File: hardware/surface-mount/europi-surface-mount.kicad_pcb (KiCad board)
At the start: 2 copper layers, 40.6 x 110 mm, 88 parts, among them J1 Conn_02x05_Odd_Even, J10 Output 6 Jack, J11 Conn_01x04_Pin, J2 Conn_01x04_Pin, J3 Output 1 Jack, J4 Output 4 Jack, J5 Analogue Input Jack, J6 Output 2 Jack, J7 Output 5 Jack, J8 Digital Input Jack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

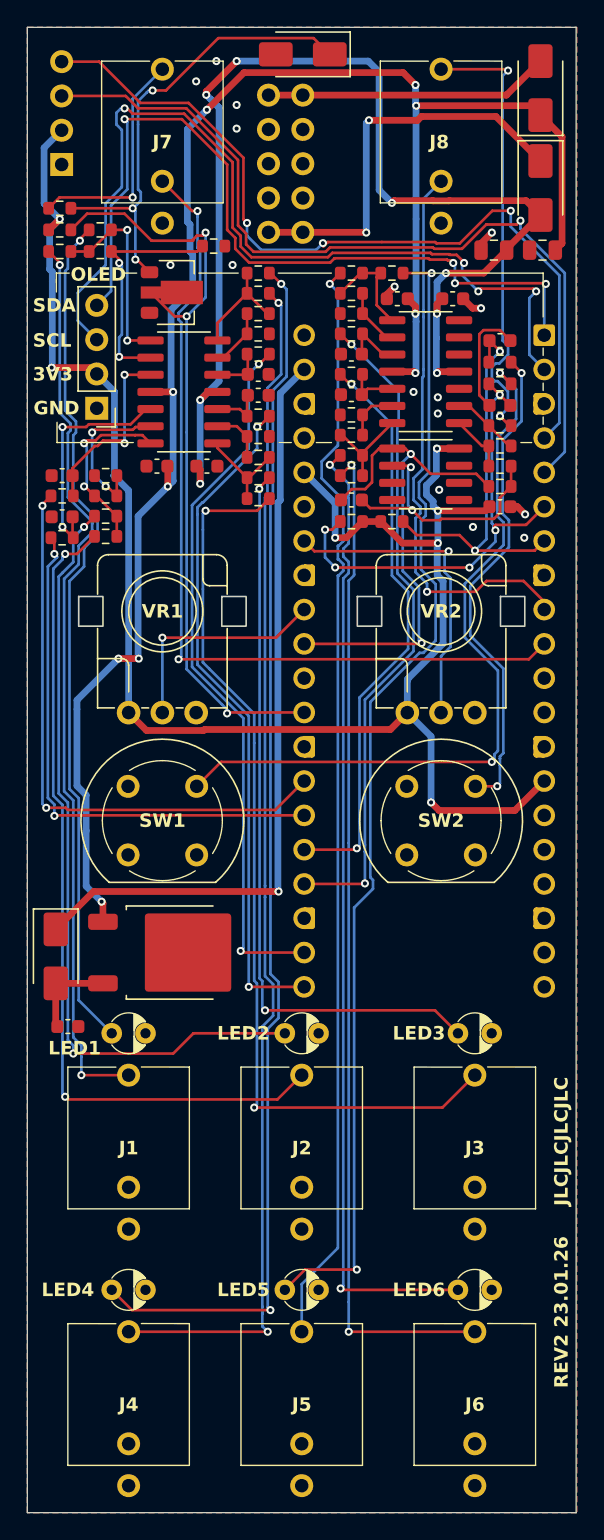
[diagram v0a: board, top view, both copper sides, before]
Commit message: Minor surface-mount PCB changes (REV 3) (#458)
* add resistors to input detect and add oshwa cert mark

* add lcsc part number to d3
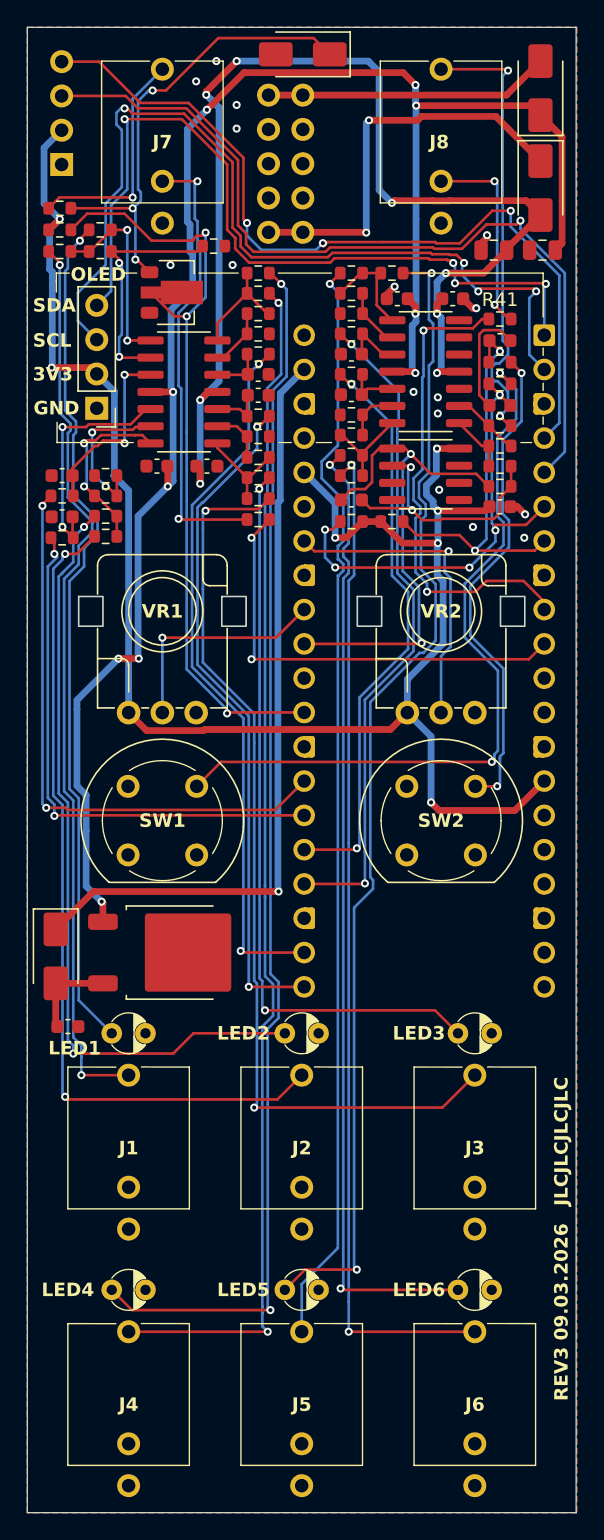
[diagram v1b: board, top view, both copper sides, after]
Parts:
- added G***: LOGO, LOGO, B.Cu at (20.3, 100.5)
- added R41: 10K, Resistor_SMD:R_0603_1608Metric, F.Cu at (35.0, 21.6)
- added R42: 10K, Resistor_SMD:R_0603_1608Metric, F.Cu at (17.1, 36.5)
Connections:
- J5 pad 2: AIN_DETECT -> Net-(J5-TN)
- J8 pad 2: DIN_DETECT -> Net-(J8-TN)
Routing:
- net Net-(J8-TN): track 0.00 -> 33.8 mm, vias 0 -> 2
- net DIN_DETECT: track 65.2 -> 33.2 mm
- net Net-(J5-TN): track 0.00 -> 14.9 mm, vias 0 -> 2
- net AIN_DETECT: track 42.2 -> 35.8 mm, vias 1 -> 2
- net GND: track 14.0 -> 13.4 mm
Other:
- board text added: "REV3 09.03.2026"
- board text added: "allensynthesis.co.uk"
- board text removed: "REV2 23.01.26"
- board text removed: "Reprogrammable Controller"
